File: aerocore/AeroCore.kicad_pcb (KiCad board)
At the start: 2 copper layers, 75 x 68 mm, 6 parts

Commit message: add firmware and pcb
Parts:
- removed 5V_Power1: Conn_01x02, TerminalBlock:TerminalBlock_Xinya_XY308-2.54-2P_1x02_P2.54mm_Horizontal
- removed ELRS1, FC1: Conn_01x04, TerminalBlock:TerminalBlock_Xinya_XY308-2.54-4P_1x04_P2.54mm_Horizontal
- removed RPi_Pico1: Pico, RPi_Pico:RPi_Pico_SMD_TH
- removed RX_SELECT1, TX_SELECT1: SN74LVC2G157DCUR, easyeda2kicad:VSSOP-8_L2.3-W2.0-P0.50-LS3.1-BL
- added 5.1k1: 5.1k, Resistor_SMD:R_0603_1608Metric_Pad0.98x0.95mm_HandSolder, F.Cu at (91.5, 48.5)
- added 5.1k2: 5.1k, Resistor_SMD:R_0603_1608Metric_Pad0.98x0.95mm_HandSolder, F.Cu at (91.5, 50.5)
- added U1: RP2040, Package_DFN_QFN:QFN-56-1EP_7x7mm_P0.4mm_EP3.2x3.2mm, F.Cu at (75.0, 73.3)
- added USBC1: USB_C_Receptacle_USB2.0_16P, Connector_USB:USB_C_Receptacle_GCT_USB4115-03-C, F.Cu at (75.2, 49.8)
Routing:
- net /POWER.GND: track 143.6 -> 0.00 mm
- net /UART0.TX: track 119.0 -> 0.00 mm
- net /UART1.RX: track 107.0 -> 0.00 mm
- net /POWER.5V: track 104.4 -> 0.00 mm
- net /UART0.RX: track 96.4 -> 0.00 mm
- net /UART1.TX: track 76.3 -> 0.00 mm
- net /UART_FC.TX: track 54.0 -> 0.00 mm
- net /UART_FC.RX: track 48.8 -> 0.00 mm
- net /SEL: track 45.6 -> 0.00 mm
- net Net-(USBC1-CC1): track 0.00 -> 18.3 mm
- net Net-(USBC1-CC2): track 0.00 -> 17.0 mm
- net /POWER.3V3: track 16.5 -> 0.00 mm
- net unconnected-(RPi_Pico1-3V3-Pad36): track 3.60 -> 0.00 mm
- net unconnected-(RPi_Pico1-GPIO8-Pad11): track 2.67 -> 0.00 mm
- net unconnected-(RPi_Pico1-GND-Pad8): track 2.25 -> 0.00 mm
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- removed copper zone on B.Cu, net /POWER.GND
- removed copper zone on F.Cu, net /POWER.GND
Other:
- board size 75 x 68 mm -> 60 x 60 mm
- board text added: "AeroNode"

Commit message: make custom rp2040 based design
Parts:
- removed 5.1k1, 5.1k2: 5.1k, Resistor_SMD:R_0603_1608Metric_Pad0.98x0.95mm_HandSolder
- removed USBC1: USB_C_Receptacle_USB2.0_16P, Connector_USB:USB_C_Receptacle_GCT_USB4115-03-C
- added BOOT1: SW_SPST, Button_Switch_SMD:SW_Push_1P1T_NO_CK_KMR2, F.Cu at (49.0, 85.5)
- added C1: 10uF, Capacitor_SMD:C_0805_2012Metric_Pad1.18x1.45mm_HandSolder, F.Cu at (54.0, 53.0)
- added C2: 10uF, Capacitor_SMD:C_0805_2012Metric_Pad1.18x1.45mm_HandSolder, F.Cu at (48.0, 59.0)
- added C3: 10uF, Capacitor_SMD:C_0805_2012Metric_Pad1.18x1.45mm_HandSolder, F.Cu at (56.5, 47.5)
- added C4: 10uF, Capacitor_SMD:C_0805_2012Metric_Pad1.18x1.45mm_HandSolder, F.Cu at (75.0, 53.0)
- added C5: 22pF, Capacitor_SMD:C_0805_2012Metric_Pad1.18x1.45mm_HandSolder, F.Cu at (75.5, 90.0)
- added C6: 22pF, Capacitor_SMD:C_0805_2012Metric_Pad1.18x1.45mm_HandSolder, F.Cu at (71.0, 85.5)
- added D1: MBR0540, Diode_SMD:D_SOD-123, F.Cu at (51.0, 47.5)
- added D2: NSR0340HT1G, Diode_SMD:D_SOD-323, F.Cu at (53.0, 85.5)
- added D3: RED, LED_SMD:LED_0603_1608Metric_Pad1.05x0.95mm_HandSolder, F.Cu at (54.4, 102.6)
- added D4: RED, LED_SMD:LED_0603_1608Metric_Pad1.05x0.95mm_HandSolder, F.Cu at (59.9, 102.5)
- added D5: ORANGE, LED_SMD:LED_0603_1608Metric_Pad1.05x0.95mm_HandSolder, F.Cu at (83.1, 49.0)
- added J1: USB_C_Receptacle_USB2.0_16P, Connector_USB:USB_C_Receptacle_Palconn_UTC16-G, F.Cu at (50.1, 74.0)
- added J2: Conn_01x03_Pin, Connector_PinHeader_2.54mm:PinHeader_1x03_P2.54mm_Horizontal, F.Cu at (93.0, 97.5)
- added J3: Conn_01x02_Pin, Connector_JST:JST_EH_S2B-EH_1x02_P2.50mm_Horizontal, B.Cu at (73.8, 49.0)
- added Q1: DMG3418L, Package_TO_SOT_SMD:SOT-23, F.Cu at (58.1, 52.0)
- added R1: 27, Resistor_SMD:R_0603_1608Metric_Pad0.98x0.95mm_HandSolder, F.Cu at (59.5, 75.5)
- added R10: 10k, Resistor_SMD:R_0603_1608Metric_Pad0.98x0.95mm_HandSolder, F.Cu at (54.0, 99.1)
- added R11: 10k, Resistor_SMD:R_0603_1608Metric_Pad0.98x0.95mm_HandSolder, F.Cu at (83.0, 52.5)
- added R12: 5.1k, Resistor_SMD:R_0603_1608Metric_Pad0.98x0.95mm_HandSolder, F.Cu at (62.5, 49.0)
- added R13: 1k, Resistor_SMD:R_0603_1608Metric_Pad0.98x0.95mm_HandSolder, F.Cu at (75.5, 82.0)
- added R2: 27, Resistor_SMD:R_0603_1608Metric_Pad0.98x0.95mm_HandSolder, F.Cu at (59.5, 72.5)
- added R3: 5.1k, Resistor_SMD:R_0603_1608Metric_Pad0.98x0.95mm_HandSolder, F.Cu at (59.5, 78.5)
- added R4: 5.1k, Resistor_SMD:R_0603_1608Metric_Pad0.98x0.95mm_HandSolder, F.Cu at (59.5, 69.5)
- added R5: 10k, Resistor_SMD:R_0603_1608Metric_Pad0.98x0.95mm_HandSolder, F.Cu at (47.5, 51.0)
- added R6: 10k, Resistor_SMD:R_0603_1608Metric_Pad0.98x0.95mm_HandSolder, F.Cu at (47.0, 55.1)
- added R7: 10k, Resistor_SMD:R_0603_1608Metric_Pad0.98x0.95mm_HandSolder, F.Cu at (82.9, 75.0)
- added R8: 10k, Resistor_SMD:R_0603_1608Metric_Pad0.98x0.95mm_HandSolder, F.Cu at (60.0, 99.1)
- added R9: 1k, Resistor_SMD:R_0603_1608Metric_Pad0.98x0.95mm_HandSolder, F.Cu at (56.0, 85.5)
- added RST1: SW_SPST, Button_Switch_SMD:SW_Push_1P1T_NO_CK_KMR2, F.Cu at (49.0, 93.5)
- added U2: AP2112K-3.3, Package_TO_SOT_SMD:SOT-23-5, F.Cu at (50.9, 55.0)
- added U3: MCP73831-2-OT, Package_TO_SOT_SMD:SOT-23-5, F.Cu at (67.1, 49.0)
- added Y2: 12MHz, Crystal:Crystal_SMD_2520-4Pin_2.5x2.0mm, F.Cu at (75.4, 85.6)
- moved U1 1.77 mm to (75.5, 75.0)
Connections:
- U1 pad 16: unconnected-(U1-GPIO13-Pad16) -> /D13
- U1 pad 17: unconnected-(U1-GPIO14-Pad17) -> /D14
- U1 pad 19: unconnected-(U1-TESTEN-Pad19) -> GND
- U1 pad 20: unconnected-(U1-XIN-Pad20) -> /XIN
- U1 pad 21: unconnected-(U1-XOUT-Pad21) -> /XOUT
- U1 pad 24: unconnected-(U1-SWCLK-Pad24) -> /SWCLK
- U1 pad 25: unconnected-(U1-SWD-Pad25) -> /SWDIO
- U1 pad 26: unconnected-(U1-RUN-Pad26) -> /~{RESET}
- U1 pad 46: unconnected-(U1-USB_DM-Pad46) -> /D-
- U1 pad 47: unconnected-(U1-USB_DP-Pad47) -> /D+
- U1 pad 56: unconnected-(U1-QSPI_SS-Pad56) -> /QSPI_CS
- U1 pad 57: unconnected-(U1-GND-Pad57) -> GND
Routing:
- net GND: track 0.00 -> 263.4 mm
- net /VBUS: track 0.00 -> 93.4 mm
- net /~{RESET}: track 0.00 -> 87.9 mm
- net /+3v3: track 0.00 -> 51.0 mm
- net /D13: track 0.00 -> 31.9 mm
- net /SWDIO: track 0.00 -> 28.4 mm
- net /D14: track 0.00 -> 27.0 mm
- net /QSPI_CS: track 0.00 -> 26.4 mm
- net Net-(D1-K): track 0.00 -> 26.0 mm
- net /VBAT: track 0.00 -> 24.7 mm
- net /D+: track 0.00 -> 24.3 mm
- net /SWCLK: track 0.00 -> 23.8 mm
- net /D-: track 0.00 -> 20.1 mm
- net Net-(USBC1-CC1): track 18.3 -> 0.00 mm
- net Net-(U3-STAT): track 0.00 -> 17.5 mm
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- added copper zone on F.Cu, net GND

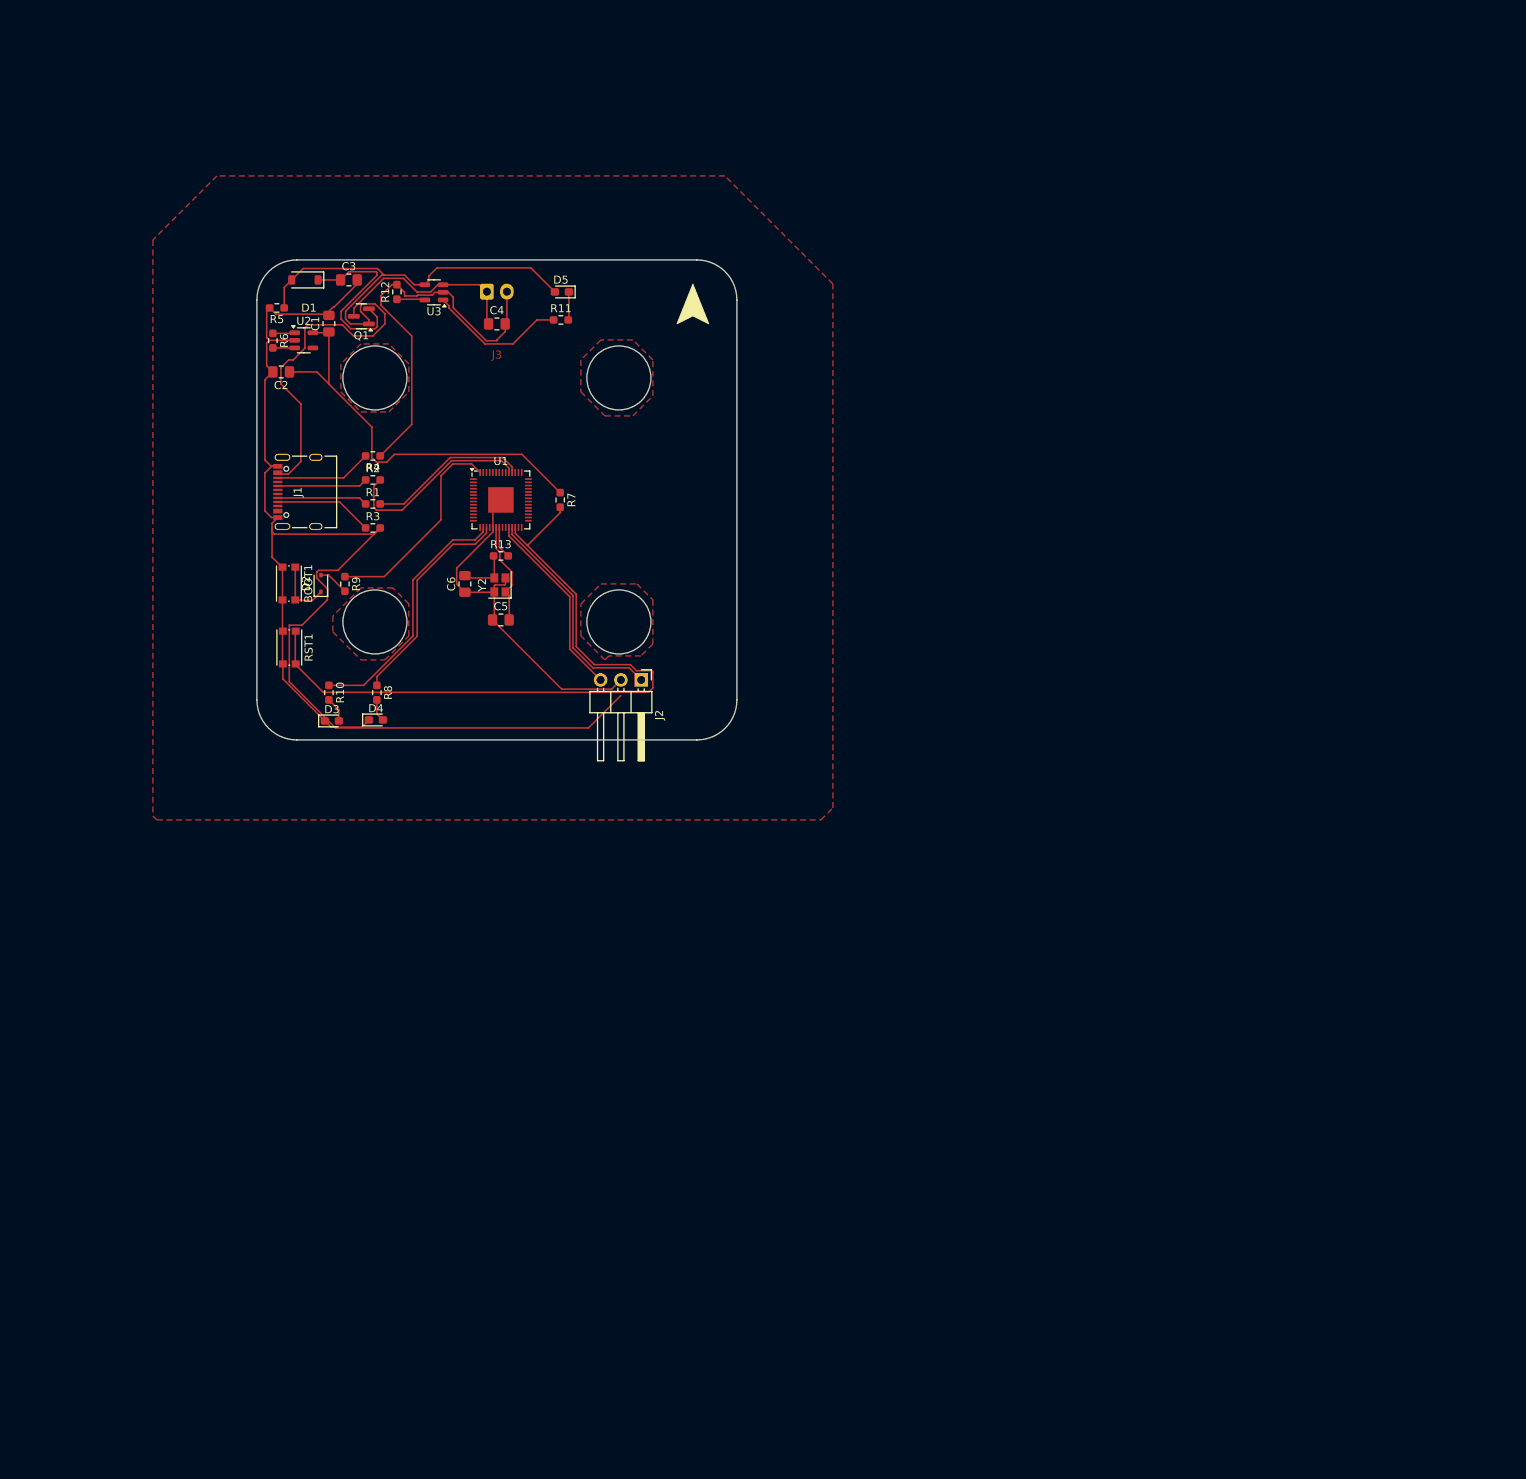
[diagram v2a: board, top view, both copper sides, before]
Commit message: add sensors to schematics
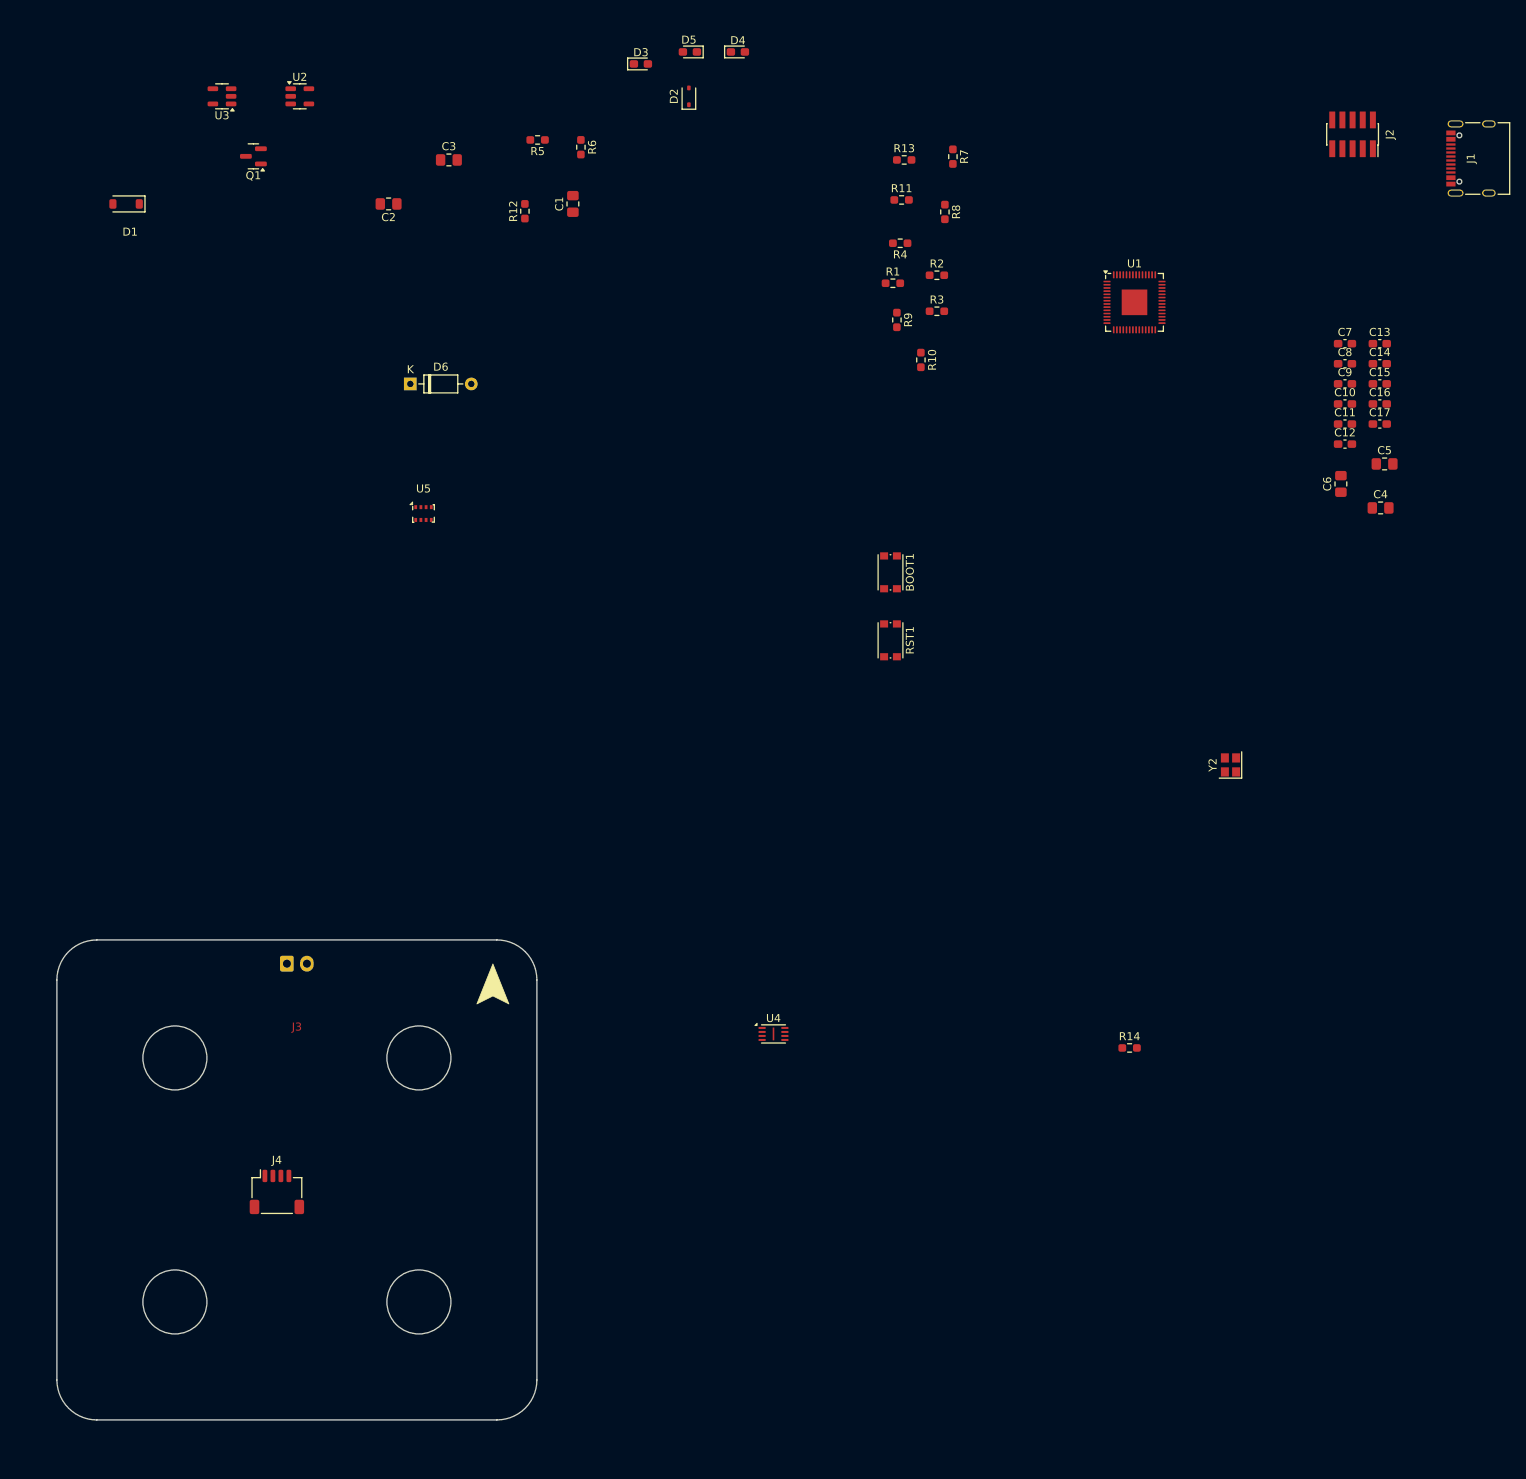
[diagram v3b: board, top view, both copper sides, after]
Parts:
- added C10: 1uF, Capacitor_SMD:C_0603_1608Metric_Pad1.08x0.95mm_HandSolder, F.Cu at (181.0, 63.0)
- added C11: 0.1uF, Capacitor_SMD:C_0603_1608Metric_Pad1.08x0.95mm_HandSolder, F.Cu at (181.0, 65.5)
- added C12: 0.1uF, Capacitor_SMD:C_0603_1608Metric_Pad1.08x0.95mm_HandSolder, F.Cu at (181.0, 68.0)
- added C13: 0.1uF, Capacitor_SMD:C_0603_1608Metric_Pad1.08x0.95mm_HandSolder, F.Cu at (185.4, 55.5)
- added C14: 0.1uF, Capacitor_SMD:C_0603_1608Metric_Pad1.08x0.95mm_HandSolder, F.Cu at (185.4, 58.0)
- added C15: 0.1uF, Capacitor_SMD:C_0603_1608Metric_Pad1.08x0.95mm_HandSolder, F.Cu at (185.4, 60.5)
- added C16: 0.1uF, Capacitor_SMD:C_0603_1608Metric_Pad1.08x0.95mm_HandSolder, F.Cu at (185.4, 63.0)
- added C17: 0.1uF, Capacitor_SMD:C_0603_1608Metric_Pad1.08x0.95mm_HandSolder, F.Cu at (185.4, 65.5)
- added C7: 1uF, Capacitor_SMD:C_0603_1608Metric_Pad1.08x0.95mm_HandSolder, F.Cu at (181.0, 55.5)
- added C8: 0.1uF, Capacitor_SMD:C_0603_1608Metric_Pad1.08x0.95mm_HandSolder, F.Cu at (181.0, 58.0)
- added C9: 0.1uF, Capacitor_SMD:C_0603_1608Metric_Pad1.08x0.95mm_HandSolder, F.Cu at (181.0, 60.5)
- added D6: 1N4148, Diode_THT:D_DO-35_SOD27_P7.62mm_Horizontal, F.Cu at (64.2, 60.5)
- added J4: Conn_01x06_Pin, Connector_JST:JST_SH_SM04B-SRSS-TB_1x04-1MP_P1.00mm_Horizontal, F.Cu at (47.5, 161.5)
- added R14: 10k, Resistor_SMD:R_0603_1608Metric_Pad0.98x0.95mm_HandSolder, F.Cu at (154.1, 143.5)
- added U4: W25Q16JVUXIQ TR, Package_SON:Winbond_USON-8-1EP_3x2mm_P0.5mm_EP0.2x1.6mm, F.Cu at (109.6, 141.8)
- added U5: BMP388, Package_LGA:Bosch_LGA-8_2x2.5mm_P0.65mm_ClockwisePinNumbering, F.Cu at (65.8, 76.7)
- J2: value Conn_01x03_Pin -> Conn_ARM_JTAG_SWD_10; footprint Connector_PinHeader_2.54mm:PinHeader_1x03_P2.54mm_Horizontal -> Connector_PinSocket_1.27mm:PinSocket_2x05_P1.27mm_Vertical_SMD
- moved J1 152.4 mm to (196.8, 32.3)
- moved C4 112.8 mm to (185.5, 76.0)
- moved C5 112.2 mm to (186.0, 70.5)
- moved J2 112.1 mm to (182.0, 29.3)
- moved C6 110.2 mm to (180.5, 73.0)
- moved D4 95.0 mm to (105.1, 19.0)
- moved Y2 94.1 mm to (166.7, 108.1)
- moved R8 93.0 mm to (131.0, 39.0)
- moved D3 90.8 mm to (93.0, 20.5)
- moved J3 87.6 mm to (48.8, 133.0)
- moved R10 84.9 mm to (128.0, 57.5)
- moved U1 83.0 mm to (154.7, 50.3)
- moved R9 76.5 mm to (125.0, 52.5)
- moved D2 76.3 mm to (99.0, 24.6)
- moved R3 75.5 mm to (130.0, 51.4)
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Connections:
- J2 pad 1: /SWDIO -> /+3v3
- J2 pad 2: GND -> /SWDIO
- J2 pad 3: /SWCLK -> GND
- R7 pad 1: /+3v3 -> /~{RESET}
- R7 pad 2: /~{RESET} -> /+3v3
- U1 pad 1: Net-(U1-IOVDD-Pad1) -> /+3v3
- U1 pad 10: Net-(U1-IOVDD-Pad1) -> /+3v3
- U1 pad 11: unconnected-(U1-GPIO8-Pad11) -> /D8
- U1 pad 12: unconnected-(U1-GPIO9-Pad12) -> /D9
- U1 pad 13: unconnected-(U1-GPIO10-Pad13) -> /D10
- U1 pad 14: unconnected-(U1-GPIO11-Pad14) -> /D11
- U1 pad 15: unconnected-(U1-GPIO12-Pad15) -> /D12
- U1 pad 18: unconnected-(U1-GPIO15-Pad18) -> /D15
- U1 pad 2: unconnected-(U1-GPIO0-Pad2) -> /D0
- U1 pad 22: Net-(U1-IOVDD-Pad1) -> /+3v3
- U1 pad 23: Net-(U1-DVDD-Pad23) -> /1.2V
- U1 pad 27: unconnected-(U1-GPIO16-Pad27) -> /D16
- U1 pad 28: unconnected-(U1-GPIO17-Pad28) -> /D17
- U1 pad 29: unconnected-(U1-GPIO18-Pad29) -> /D18
- U1 pad 3: unconnected-(U1-GPIO1-Pad3) -> /D1
- U1 pad 30: unconnected-(U1-GPIO19-Pad30) -> /D19
- U1 pad 31: unconnected-(U1-GPIO20-Pad31) -> /D20
- U1 pad 32: unconnected-(U1-GPIO21-Pad32) -> /D21
- U1 pad 33: Net-(U1-IOVDD-Pad1) -> /+3v3
- U1 pad 34: unconnected-(U1-GPIO22-Pad34) -> /D22
- U1 pad 35: unconnected-(U1-GPIO23-Pad35) -> /D23
- U1 pad 36: unconnected-(U1-GPIO24-Pad36) -> /D24
- U1 pad 37: unconnected-(U1-GPIO25-Pad37) -> /D25
- U1 pad 38: unconnected-(U1-GPIO26_ADC0-Pad38) -> /A0
- U1 pad 39: unconnected-(U1-GPIO27_ADC1-Pad39) -> /A1
- U1 pad 4: unconnected-(U1-GPIO2-Pad4) -> /D2
- U1 pad 40: unconnected-(U1-GPIO28_ADC2-Pad40) -> /A2
- U1 pad 41: unconnected-(U1-GPIO29_ADC3-Pad41) -> /A3
- U1 pad 42: Net-(U1-IOVDD-Pad1) -> /+3v3
- U1 pad 43: unconnected-(U1-ADC_AVDD-Pad43) -> /+3v3
- U1 pad 44: unconnected-(U1-VREG_IN-Pad44) -> /+3v3
- U1 pad 45: unconnected-(U1-VREG_VOUT-Pad45) -> /1.2V
- U1 pad 48: unconnected-(U1-USB_VDD-Pad48) -> /+3v3
- U1 pad 49: Net-(U1-IOVDD-Pad1) -> /+3v3
- U1 pad 5: unconnected-(U1-GPIO3-Pad5) -> /D3
- U1 pad 50: Net-(U1-DVDD-Pad23) -> /1.2V
- U1 pad 51: unconnected-(U1-QSPI_SD3-Pad51) -> /QSPI_D3
- U1 pad 52: unconnected-(U1-QSPI_SCLK-Pad52) -> /QSPI_CLK
- U1 pad 53: unconnected-(U1-QSPI_SD0-Pad53) -> /QSPI_D0
- U1 pad 54: unconnected-(U1-QSPI_SD2-Pad54) -> /QSPI_D2
- U1 pad 55: unconnected-(U1-QSPI_SD1-Pad55) -> /QSPI_D1
- U1 pad 6: unconnected-(U1-GPIO4-Pad6) -> /D4
- U1 pad 7: unconnected-(U1-GPIO5-Pad7) -> /D5
- U1 pad 8: unconnected-(U1-GPIO6-Pad8) -> /D6
- U1 pad 9: unconnected-(U1-GPIO7-Pad9) -> /D7
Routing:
- net GND: track 263.4 -> 0.00 mm
- net /VBUS: track 93.4 -> 0.00 mm
- net /~{RESET}: track 87.9 -> 0.00 mm
- net /+3v3: track 51.0 -> 0.00 mm
- net /D13: track 31.9 -> 0.00 mm
- net /SWDIO: track 28.4 -> 0.00 mm
- net /D14: track 27.0 -> 0.00 mm
- net /QSPI_CS: track 26.4 -> 0.00 mm
- net Net-(D1-K): track 26.0 -> 0.00 mm
- net /VBAT: track 24.7 -> 0.00 mm
- net /D+: track 24.3 -> 0.00 mm
- net /SWCLK: track 23.8 -> 0.00 mm
- net /D-: track 20.1 -> 0.00 mm
- net Net-(U3-STAT): track 17.5 -> 0.00 mm
- net /XIN: track 12.9 -> 0.00 mm
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- removed copper zone on F.Cu, net GND
